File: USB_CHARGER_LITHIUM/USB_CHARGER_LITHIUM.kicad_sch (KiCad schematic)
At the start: 21 parts, among them J1 USB4135, J2 Conn_01x02, J3 Conn_01x02, U1 TP5000X-4.2-ESOP8, U2 XB7608A

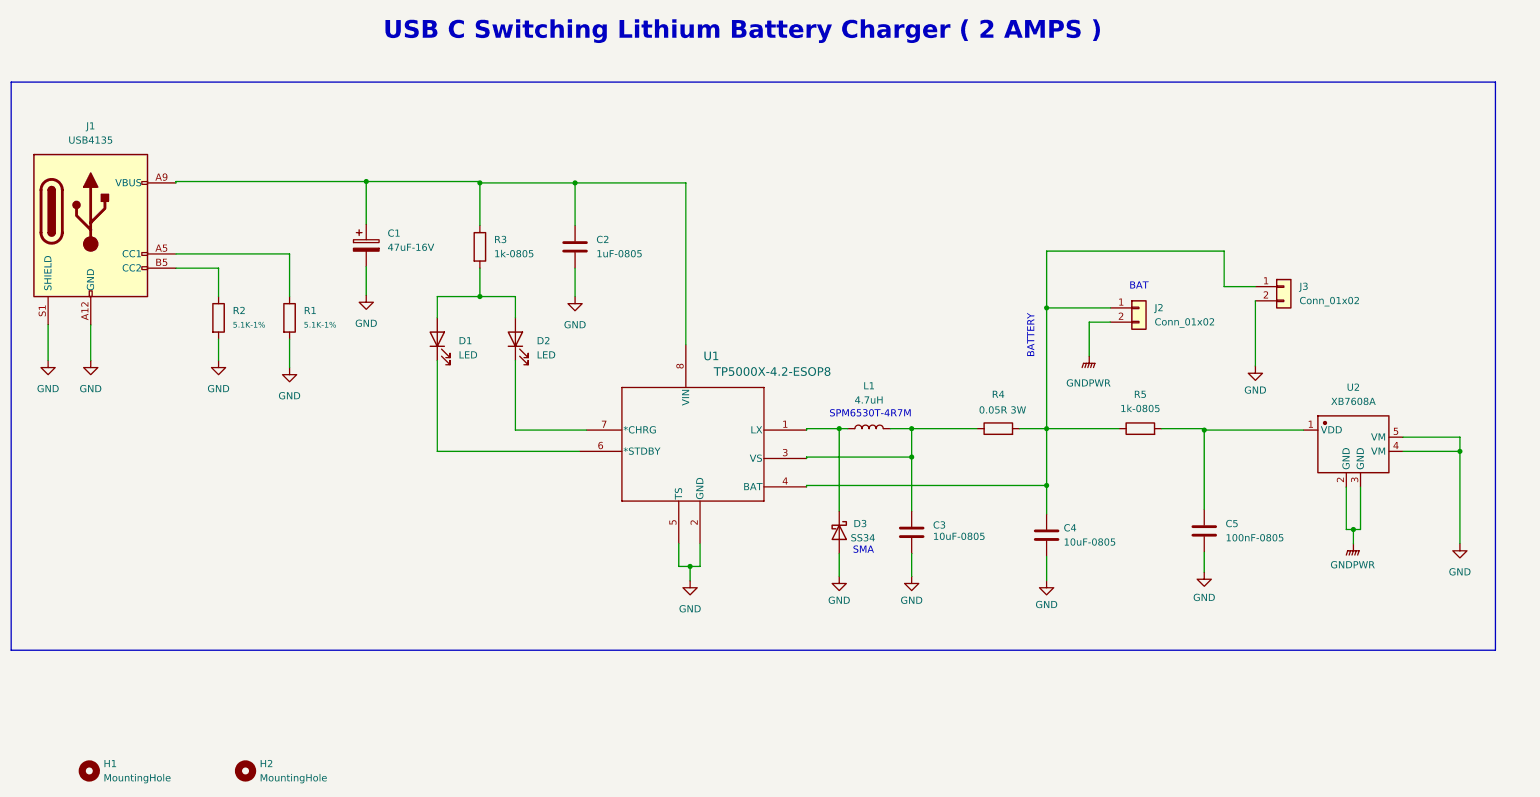
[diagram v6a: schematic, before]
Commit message: Fixed shchematic grid and added ground copper planes
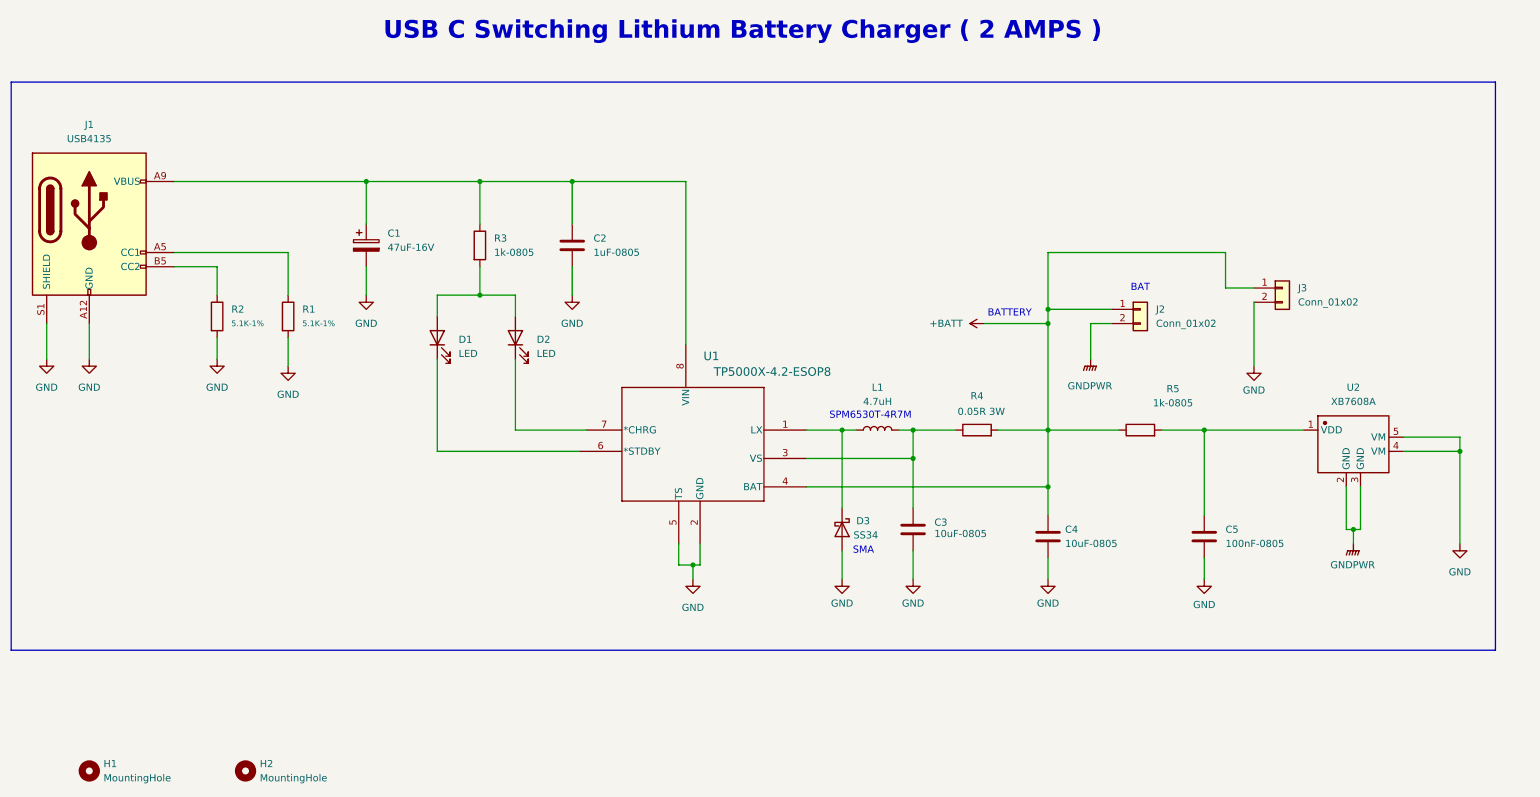
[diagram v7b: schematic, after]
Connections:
- net +BATT: now reaches C4.1, J2.1 (Pin_1), J3.1 (Pin_1), R4.2, R5.1, U1.4 (BAT)
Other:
- moved on the sheet: C2, C3, C5, D3, L1, R4

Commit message: Finished pcb design. Working on BOM and Positions
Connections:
- net VBUS: now reaches C1.1, C2.1, J1.A9 (VBUS), J1.B9 (VBUS), R3.1, U1.8 (VIN)
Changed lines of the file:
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@@
+	)
+	(junction
+		(at 49.53 48.26)
+		(diameter 0)
+		(color 0 0 0 0)
 	)
 	(junction
@@
 	(wire
 		(pts
-			(xy 45.72 48.26) (xy 80.01 48.26)
+			(xy 45.72 48.26) (xy 49.53 48.26)
 		)
 		(stroke
@@
 		(pts
 			(xy 80.01 48.26) (xy 100.33 48.26)
+		)
+		(stroke
+			(width 0)
+			(type default)
+		)
+	)
+	(wire
+		(pts
+			(xy 49.53 48.26) (xy 80.01 48.26)
 		)
 		(stroke
@@
 	(wire
 		(pts
+			(xy 49.53 44.45) (xy 49.53 48.26)
+		)
+		(stroke
+			(width 0)
+			(type default)
+		)
+	)
+	(wire
+		(pts
 			(xy 201.93 92.71) (xy 214.63 92.71)
 		)
@@
 					(unit 1)
 				)
+			)
+		)
+	)
+	(symbol
+		(lib_id "power:VBUS")
+		(at 49.53 44.45 0)
+		(unit 1)
+		(exclude_from_sim no)
+		(in_bom yes)
+		(on_board yes)
+		(dnp no)
+		(fields_autoplaced yes)
+		(property "Reference" "#PWR017"
+			(at 49.53 48.26 0)
+			(effects
+				(font
+					(size 1.27 1.27)
+				)
+				(hide yes)
+			)
+		)
+		(property "Value" "VBUS"
+			(at 49.53 39.37 0)
+			(effects
+				(font
+					(size 1.27 1.27)
+				)
+			)
+		)
+		(property "Footprint" ""
+			(at 49.53 44.45 0)
+			(effects
+				(font
+					(size 1.27 1.27)
+				)
+				(hide yes)
+			)
+		)
+		(property "Datasheet" ""
+			(at 49.53 44.45 0)
+			(effects
+				(font
+					(size 1.27 1.27)
+				)
+				(hide yes)
+			)
+		)
+		(property "Description" "Power symbol creates a global label with name \"VBUS\""
+			(at 49.53 44.45 0)
+			(effects
+				(font
+					(size 1.27 1.27)
+				)
+				(hide yes)
+			)
+		)
+		(pin "1"
+		)
+		(instances
+			(project ""
+				(path "/740b141e-76db-4770-b8b7-f30b8f055222"
+					(reference "#PWR017")
+					(unit 1)
+				)
